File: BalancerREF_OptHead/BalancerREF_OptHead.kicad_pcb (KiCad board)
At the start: 2 copper layers, 25 x 50 mm, 24 parts, among them J5 TO MAIN BOARD, Q1 AO3400A, U4 TS3021IYLT, U8 TLV9062IDR

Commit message: feat: fiducials, net classes, and a BAT sense divider
Fiducials (1 mm dot / 2 mm mask), three per populated face at three of the
four corners - never four, since a symmetric set gives the placement machine
no way to distinguish a 180-degree-rotated panel. Main board gets both faces
(FID1-3 front, FID4-6 back); the optical head is single-sided so its back has
none.

Net classes set in both .kicad_pro, sized from IPC-2221 at 1 oz outer copper
and a 10 C rise (0.20 mm ~ 0.74 A, 0.50 ~ 1.45 A, 0.80 ~ 2.03 A):
  Default 0.20  Power 0.50  Switch 0.80 (main)  Emitter 0.80 (head)  USB pair
Switch clearance stays at 0.20 rather than 0.25: the TPS63031's WSON-10 puts
its own L1/L2 pads 0.20 mm from its thermal pad, so anything stricter fails
inside the package. The USB class exists for tuning and length matching but is
not an impedance solution - that needs the fab's stackup. The S3's native USB
is Full Speed, so it matters less than it would at High Speed.

BAT sense divider - R33/R34 (1M) and C31 (100n) on GPIO4 (ADC1_CH3):
SUPPLY_SENSE reads SYS_SW/2 and cannot separate USB from battery, because a
USB port at the low end of spec minus D2's drop lands near 4.30 V against a
full cell at 4.20 V - inside divider tolerance plus ADC error. Comparing
SYS_SW against BAT is a differential test and separates them cleanly. 1M/1M
rather than 100k/100k because this divider hangs on the cell even when the
puck is off (~2 uA vs ~21 uA); the resulting 500k source impedance means
firmware needs a long sample time and multisample.

U1 pin 8's no-connect removed and U1.8 dropped from unused-pins.json.

verify_netlist.py spec extended with BAT_SENSE and the new ground/BAT members.
  main PASS: 44 exact circuit nets, 286 pin endpoints, 128 IC pads
  head PASS: 16 exact circuit nets, 63 pin endpoints
ERC 0 errors. DRC: main 2 (U1 library courtyard vs the corner holes), head 0.
All 81 schematic parts confirmed present on the board; the only board-only
refs are the 6 fiducials and 4 mounting hole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
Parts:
- added FID1: FIDUCIAL, Fiducial_1mm_Mask2mm, F.Cu at (121.5, 146.5)
- added FID2: FIDUCIAL, Fiducial_1mm_Mask2mm, F.Cu at (103.5, 103.5)
- added FID3: FIDUCIAL, Fiducial_1mm_Mask2mm, F.Cu at (121.5, 103.5)

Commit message: fix: address repo review findings before routing
An external review raised seven pre-routing items plus smaller notes. Each was
checked against the manufacturer source rather than taken on faith; two did not
survive that check and are recorded as not-confirmed.

Confirmed and fixed:

  * D1 peak current. The head runs from SYS_SW, and with the BQ24075 regulating
    OUT to 5.5 V, R18 at 3.0 ohm gave ~1.1 A peak against D1's 1 A absolute
    maximum. The BOM note had only checked the 4.2 V battery case, and the
    charger swap - which replaced a Schottky holding SYS near 4.55 V - is what
    pushed it over. R18 -> 3.9 ohm: ~0.49 A at a full cell (the bench-set design
    point) and ~0.90 A worst case at 5.5 V with a low-Vf bin.
  * Charger stuck at USB100. EN1/EN2 have 285k internal pulldowns and nothing
    drove them, so the input limit covered system load AND charge current at
    100 mA. setupCharger() now selects USB500 at boot, and status reports
    input_present/charging from PGOOD and CHG.
  * U9 input transition rate. R29/C26 fed the SN74LVC1G08 a 0.47 us edge against
    a 10 ns/V spec, ~25x out. Swapped to SN74LVC1G132, a Schmitt NAND with the
    identical SOT-23-5 pinout (verified against SLVS322 Figure 4-1), which
    conditions both inputs. It inverts, so U10's trigger moved from B rising to
    ~A falling - the SN74LVC1G123 supports both edges.
  * Switcher parts on the wrong face. L1 and C4-C7 were on the back with U6 on
    the front, putting vias in a 2.4 MHz switching loop. Moved to the front;
    C2/C3/C30 followed for the BQ24075. The "ICs front, passives back" rule does
    not survive contact with a switching converter.
  * U1 decoupling. C8 is now 0.38 mm from the 3V3 pad instead of ~9 mm. Both
    stay on the back, since U1's body owns that part of the front.
  * Head board emitter loop, was spanning the full board width. C20/R18/Q1 now
    cluster in 6.9 x 3.3 mm. R21/C21 went from 4 mm off Q1 to 16 mm and sit
    3.6/3.9 mm from U8 pins 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
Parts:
- R18: value 3R0 1206 0.5W -> 3R9 1206 0.5W
- moved R25 12.9 mm to (115.0, 132.1)
- moved R24 12.5 mm to (115.8, 134.4)
- moved Q1 12.0 mm to (115.3, 121.6)
- moved R18 9.09 mm to (112.3, 118.2)
- moved C20 5.75 mm to (108.5, 121.4)
- moved R21 5.30 mm to (103.2, 132.1)
- moved C21 3.76 mm to (103.0, 134.3)
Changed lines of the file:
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@@
 	(footprint "R_0603_1608Metric"
 		(layer "F.Cu")
-		(at 103.325 126.825)
+		(at 103.231308 132.124733)
 		(descr "Resistor SMD 0603 (1608 Metric), square (rectangular) end terminal, IPC-7351 nominal, (Body size source: IPC-SM-782 page 72, https://www.pcb-3d.com/wordpress/wp-content/uploads/ipc-sm-782a_amendment_1_and_2.pdf)")
 		(tags "resistor")
@@
 	(footprint "R_0603_1608Metric"
 		(layer "F.Cu")
-		(at 103.325 133.825)
+		(at 115.825 134.424999)
 		(descr "Resistor SMD 0603 (1608 Metric), square (rectangular) end terminal, IPC-7351 nominal, (Body size source: IPC-SM-782 page 72, https://www.pcb-3d.com/wordpress/wp-content/uploads/ipc-sm-782a_amendment_1_and_2.pdf)")
 		(tags "resistor")
@@
 	(footprint "SOT-23"
 		(layer "F.Cu")
-		(at 103.324999 122.625)
+		(at 115.325 121.57141)
 		(descr "SOT, 3 Pin (JEDEC TO-236 Var AB https://www.jedec.org/document_search?search_api_views_fulltext=TO-236)")
 		(tags "SOT TO_SOT_SMD")
@@
 	(footprint "R_1206_3216Metric"
 		(layer "F.Cu")
-		(at 121.412867 118.537132)
+		(at 112.325 118.225)
 		(descr "Resistor SMD 1206 (3216 Metric), square (rectangular) end terminal, IPC-7351 nominal, (Body size source: IPC-SM-782 page 72, https://www.pcb-3d.com/wordpress/wp-content/uploads/ipc-sm-782a_amendment_1_and_2.pdf)")
 		(tags "resistor")
@@
 			)
 		)
-		(property "Value" "3R0 1206 0.5W"
+		(property "Value" "3R9 1206 0.5W"
 			(at 0 1.83 0)
 			(layer "F.Fab")
@@
 	(footprint "R_0603_1608Metric"
 		(layer "F.Cu")
-		(at 103.112867 137.037132)
+		(at 115.026218 132.094884)
 		(descr "Resistor SMD 0603 (1608 Metric), square (rectangular) end terminal, IPC-7351 nominal, (Body size source: IPC-SM-782 page 72, https://www.pcb-3d.com/wordpress/wp-content/uploads/ipc-sm-782a_amendment_1_and_2.pdf)")
 		(tags "resistor")
@@
 	(footprint "C_1210_3225Metric"
 		(layer "F.Cu")
-		(at 103.325 118.844615)
+		(at 108.470708 121.401711)
 		(descr "Capacitor SMD 1210 (3225 Metric), square (rectangular) end terminal, IPC-7351 nominal, (Body size source: IPC-SM-782 page 76, https://www.pcb-3d.com/wordpress/wp-content/uploads/ipc-sm-782a_amendment_1_and_2.pdf)")
 		(tags "capacitor")
@@
 	(footprint "C_0805_2012Metric"
 		(layer "F.Cu")
-		(at 103.112867 130.537132)
+		(at 103.030788 134.296969)
 		(descr "Capacitor SMD 0805 (2012 Metric), square (rectangular) end terminal, IPC-7351 nominal, (Body size source: IPC-SM-782 page 76, https://www.pcb-3d.com/wordpress/wp-content/uploads/ipc-sm-782a_amendment_1_and_2.pdf, https://docs.google.com/spreadsheets/d/1BsfQQcO9C6DZCsRaXUlFlo91Tg2WpOkGARC1WS5S8t0/edit?usp=sharing)")
 		(tags "capacitor")

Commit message: fix: flip PD1 - the optical comparator could never trip
Confirmed against the netlist, not the description. PD1 was wired cathode to
+3V3 and anode to the transimpedance summing node. The reverse bias is correct
that way, 1.65 V cathode-positive, which is presumably why it survived this long.
The signal direction is not.

Photocurrent leaves the ANODE of a reverse-biased photodiode, so with the anode
on the summing node it was injected into the node rather than pulled out:

  PD1 anode on the node  -> current INTO the summing node
  U8A, U8.2 = IN-        -> inverting TIA, TIA_OUT FALLS
  U8B, gain -120k/10k    -> inverting, OPT_AMP RISES from 1.65 V
  U4, U8.4 = IN-         -> against CMP_THRESHOLD on IN+

CMP_THRESHOLD is 3.3 * 10k/(22k+10k) = 1.016 V with the output low, 1.064 V with
it high - R28's 470k gives 48 mV of hysteresis in the correct direction.
OPT_AMP idles at 1.65 V, AC-coupled to the 1.65 V reference, so it sits 634 mV
ABOVE the threshold and light drove it further away. IN- stayed above IN+ at any
illumination and the output never left its low state. With the Rev F NAND gating
that is total: U9 never falls, U10 never triggers, TR-VERT had no tach at all.

Flipping the diode fixes the chain without touching anything else. Cathode to
PD_TIA_IN, anode to GND: same 1.65 V reverse bias, photocurrent now pulled out of
the node, TIA_OUT rises, OPT_AMP falls through 1.016 V, comparator trips. It
takes about 5.3 uA of photocurrent - 634 mV / 12 / 10k.

Side effect worth having, since Rev F moved Q1 nearer PD1 when it tightened the
emitter loop: the emitter turn-off edge lands inside the synchronous gate window
and cannot be rejected, and after the flip its coupling into the summing node
pushes TIA_OUT the same way darkness does, away from the trip point.

Why none of the existing checks found it. verify_head.py compares the exported
netlist against exact net membership and passed throughout - netlist matched
spec, board matched netlist, ERC clean - because 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
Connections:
- PD1 pad 1: /+3V3 -> /PD_TIA_IN
- PD1 pad 2: /PD_TIA_IN -> GND
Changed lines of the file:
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@@
 			(layers "F.Cu" "F.Mask")
 			(roundrect_rratio 0.125)
-			(net "/+3V3")
+			(net "/PD_TIA_IN")
 		)
 		(pad "2" smd roundrect
@@
 			(layers "F.Cu" "F.Mask")
 			(roundrect_rratio 0.125)
-			(net "/PD_TIA_IN")
+			(net "GND")
 		)
 		(embedded_fonts no)

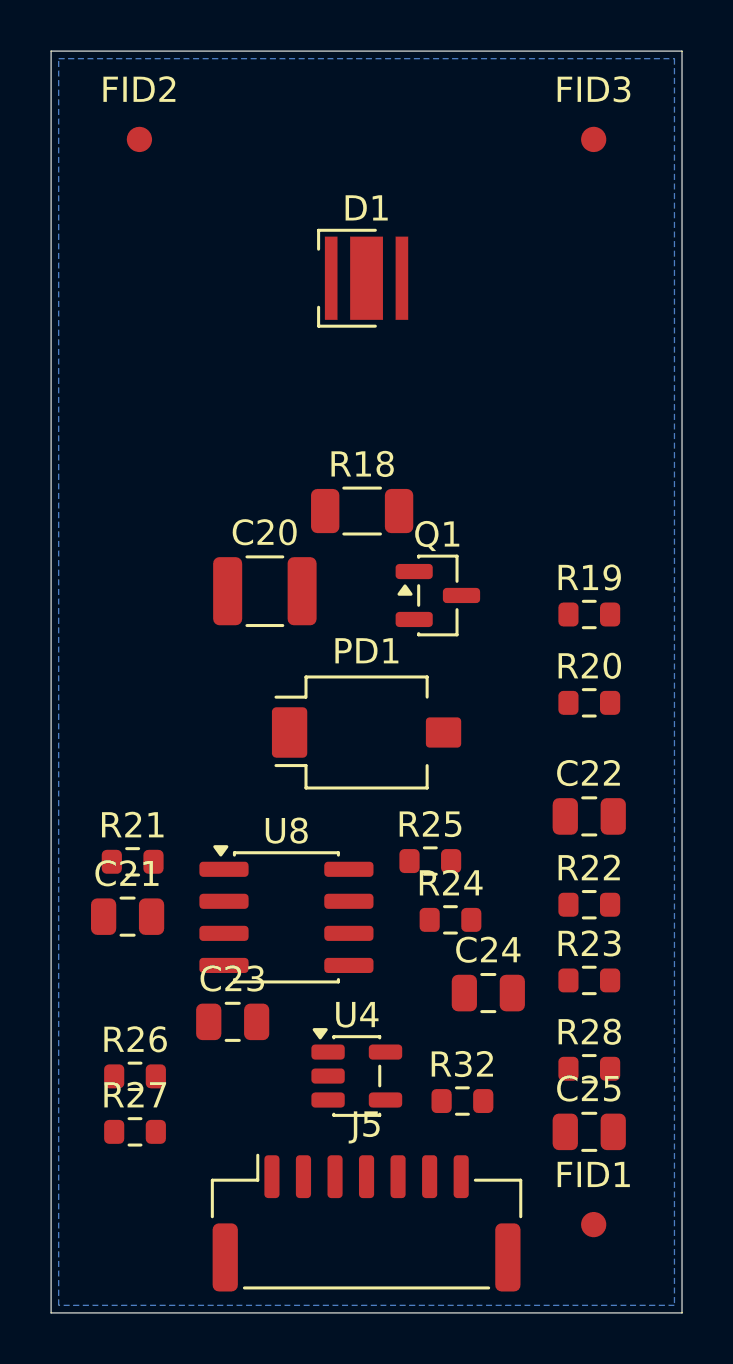
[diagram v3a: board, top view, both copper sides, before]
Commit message: feat: optical head rewired in signal-chain order and regrouped for routing
Schematic: components laid out left to right along the signal path and
joined with real wires instead of labelled stubs. One net label per wired
net keeps the PCB's net names. Symbol UUIDs, values and footprints are
untouched. verify_head.py passes and ERC is clean.

Board: pulse loop (C20/R18/Q1/R19/R20) top-left away from PD1's summing
node, TIA and gain stage right of centre, comparator above the connector.
D1 and PD1 stay on the centreline; a BAFFLE rule area (y 116.5 to 124.2,
footprints only) with silk marks reserves the band for the printed
divider. The existing back-side GND pour is unchanged.

Scripts: rewire_head.py and regroup_head.py, both reproducible.

Co-Authored-By: Claude Fable 5.1 <noreply@anthropic.com>
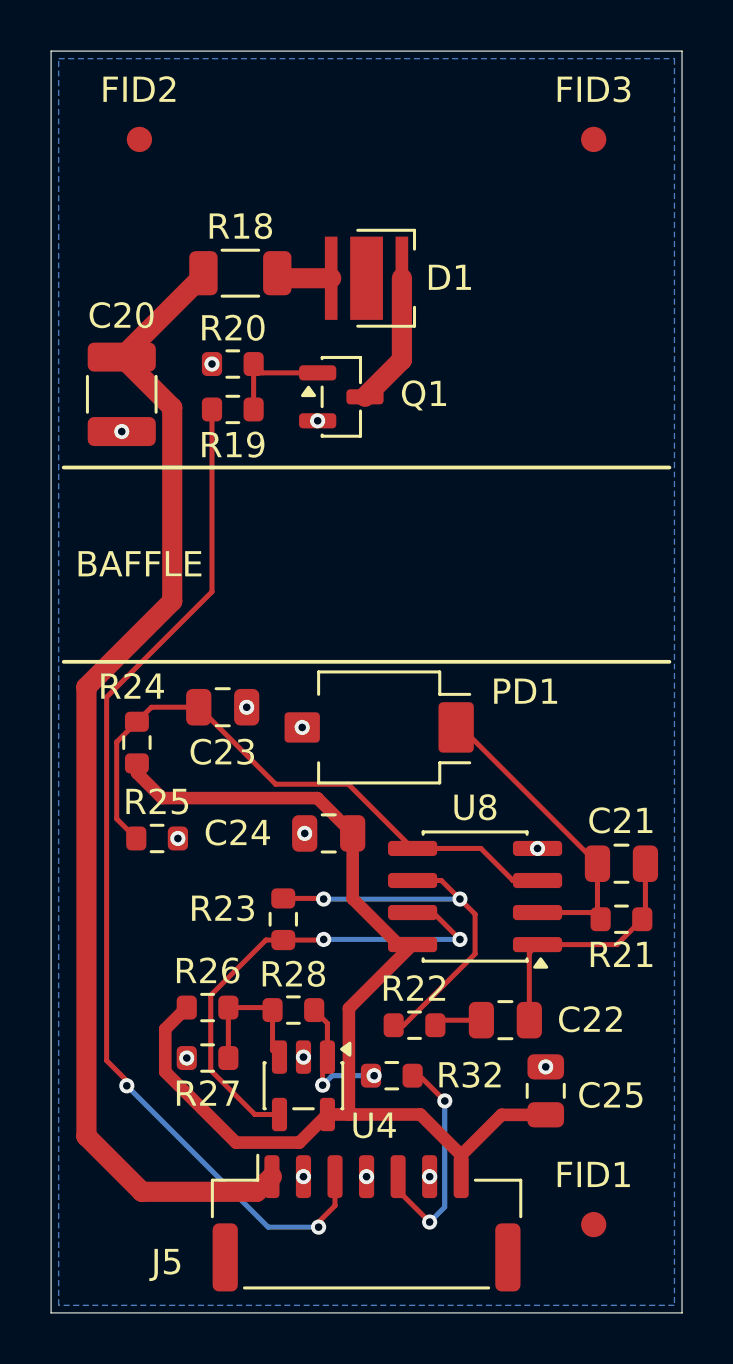
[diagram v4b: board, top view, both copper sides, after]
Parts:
- moved C21 19.7 mm to (122.6, 132.2)
- moved R21 19.5 mm to (122.6, 134.4), turned to 180 degrees
- moved R20 19.5 mm to (107.2, 112.4), turned to 180 degrees
- moved R19 16.3 mm to (107.2, 114.2), turned to 180 degrees
- moved R24 14.3 mm to (103.4, 127.4), turned to 90 degrees
- moved C23 12.5 mm to (106.8, 126.0)
- moved R23 12.4 mm to (109.2, 134.4), turned to 90 degrees
- moved R28 12.0 mm to (109.6, 138.0), turned to 180 degrees
- moved R25 10.9 mm to (104.2, 131.2)
- moved R18 10.6 mm to (107.5, 108.8)
- moved C20 9.64 mm to (102.8, 113.6), turned to -90 degrees
- moved C24 8.94 mm to (111.0, 131.0), turned to 180 degrees
- moved Q1 8.75 mm to (111.5, 113.7)
- moved C22 8.73 mm to (118.0, 138.4), turned to 180 degrees
- moved R22 8.41 mm to (114.4, 138.6)
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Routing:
- net /SYS_SW: track 0.00 -> 46.3 mm
- net /+3V3: track 0.00 -> 45.2 mm
- net /OPT_LED_EN: track 0.00 -> 41.0 mm, vias 0 -> 2
- net /OPT_VREF: track 0.00 -> 24.2 mm
- net /OPT_AMP: track 0.00 -> 19.5 mm, vias 0 -> 2
- net /AMP_INV: track 0.00 -> 16.0 mm, vias 0 -> 2
- net /PD_TIA_IN: track 0.00 -> 12.7 mm
- net /TIA_OUT: track 0.00 -> 9.95 mm
- net /OPT_COMP: track 0.00 -> 9.06 mm, vias 0 -> 2
- net /CMP_THRESHOLD: track 0.00 -> 5.77 mm
- net /CMP_OUT: track 0.00 -> 5.59 mm, vias 0 -> 2
- net Net-(D1-K): track 0.00 -> 5.31 mm
- net /MOS_GATE: track 0.00 -> 4.48 mm
- net Net-(D1-A): track 0.00 -> 2.22 mm
- net /AC_COUPLED: track 0.00 -> 1.91 mm
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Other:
- board text added: "BAFFLE"

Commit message: chore: update balancer board files and review tooling
Co-Authored-By: Claude Opus 5 (1M context) <noreply@anthropic.com>
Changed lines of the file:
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@@
 		)
 		(embedded_fonts no)
-		(model "${KICAD10_3DMODEL_DIR}/LED_SMD.3dshapes/LED_Cree-XP.step"
+		(model "${KIPRJMOD}/3dmodels/LED_Cree-XP.step"
 			(offset
 				(xyz 0 0 0)
@@
 		)
 		(embedded_fonts no)
-		(model "${KICAD10_3DMODEL_DIR}/OptoDevice.3dshapes/Osram_BPW34S-SMD.step"
+		(model "${KIPRJMOD}/3dmodels/BPW34S.step"
 			(offset
 				(xyz 0 0 0)
@@
 	)
 	(gr_text "BAFFLE"
-		(at 103.5 120.35 0)
+		(at 112 120.65 0)
 		(layer "F.SilkS")
 		(effects

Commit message: fix: BOM fields, silkscreen labels, +3V3 plane, and stale docs before review
- MPN fields: R3/R35/R36 (were "100k"), U9 (was the 1G08), R18 (was 3R0)
- Title block: HOBOVibe spelling; head company line no longer says "human
  review required"
- C20 on the head board rated 10 V; SYS_SW can sit at 5.5 V
- Silkscreen: board name and rev on both boards, battery and MAG polarity,
  pin-1 marks on J4 and both J5
- Main PCB: SYS, SYS_SW, BAT and USB_VBUS tracks removed from In2.Cu so the
  +3V3 plane is whole; three vias that only served them removed. Those four
  nets need re-routing on the outer layers.
- Docs: routing state, ground-pour wording, missing head-board holes,
  JLCPCB parts table rebuilt for the Rev F BOM, superseded LIS2DW12 and
  phototransistor sections marked in DATASHEET-VERIFICATION

Not done here (no KiCad in this environment): re-export of PDF/netlist/ERC/DRC.

Co-Authored-By: Claude Fable 5.1 <noreply@anthropic.com>
Claude-Session: https://claude.ai/code/session_01JeUyuyqf13Zf6V8TjfofPH
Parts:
- C20: value 100u / 6.3V -> 100u / 10V
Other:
- board text added: "1"
- board text added: "OPTHEAD RevB"
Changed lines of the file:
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@@
 			)
 		)
-		(property "Value" "100u / 6.3V"
+		(property "Value" "100u / 10V"
 			(at 0 2.3 90)
 			(layer "F.Fab")
@@
 			)
 		)
+	)
+	(gr_text "OPTHEAD RevB"
+		(at 112.5 104.0 0)
+		(layer "F.SilkS")
+		(effects
+			(font
+				(size 0.9 0.9)
+				(thickness 0.13)
+			)
+		)
+	)
+	(gr_text "1"
+		(at 107.5 144.6 0)
+		(layer "F.SilkS")
+		(effects
+			(font
+				(size 0.6 0.6)
+				(thickness 0.1)
+			)
+		)
